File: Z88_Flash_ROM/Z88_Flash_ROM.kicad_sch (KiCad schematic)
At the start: 3 parts, among them J1 Conn_01x03, U1 SST39SF040, U2 Z88_ROM

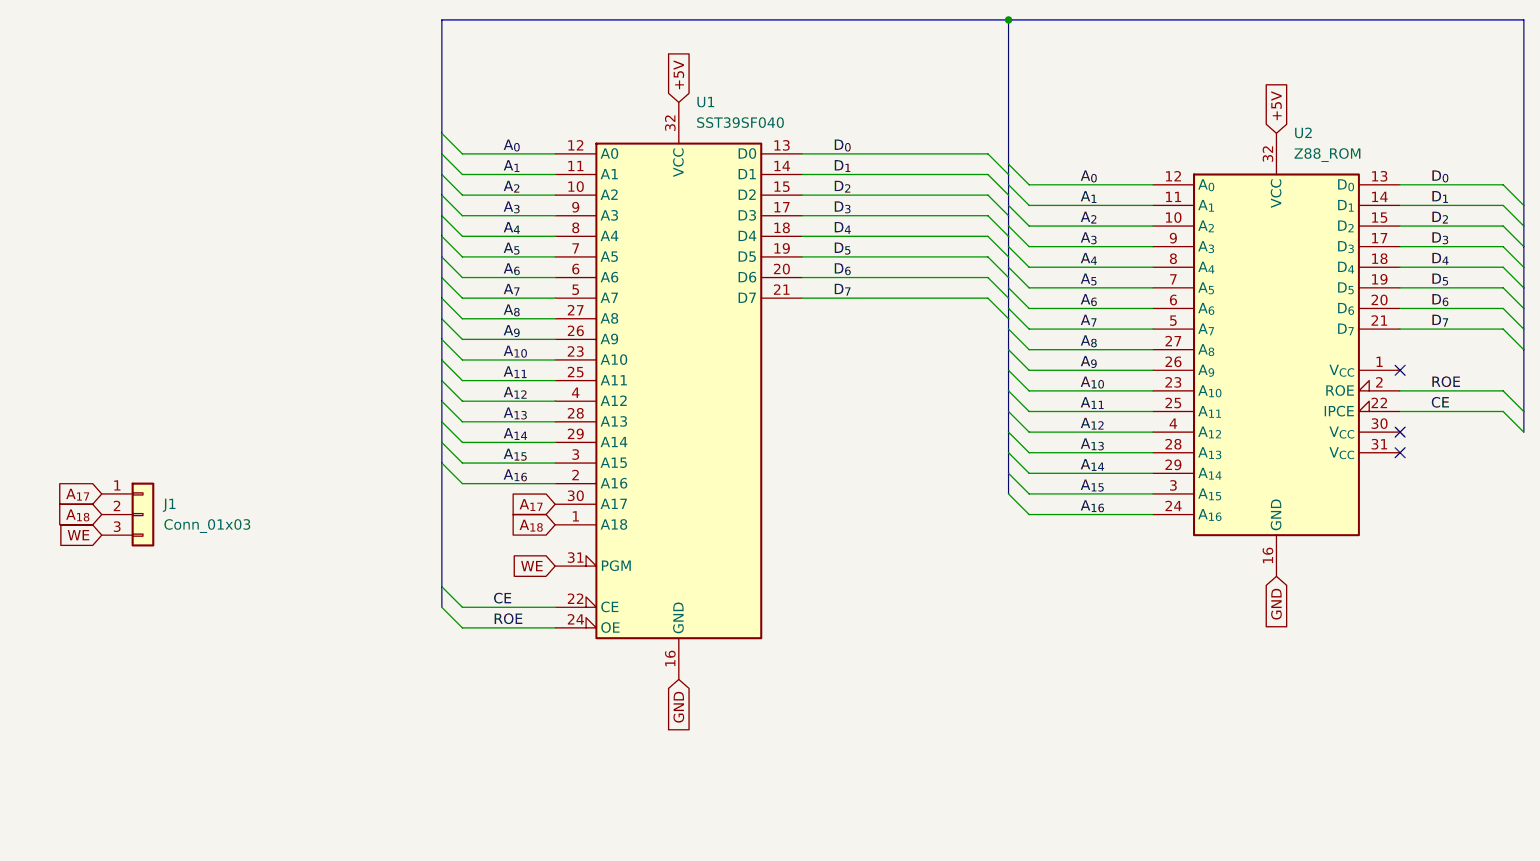
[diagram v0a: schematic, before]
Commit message: Reduced PCB thickness
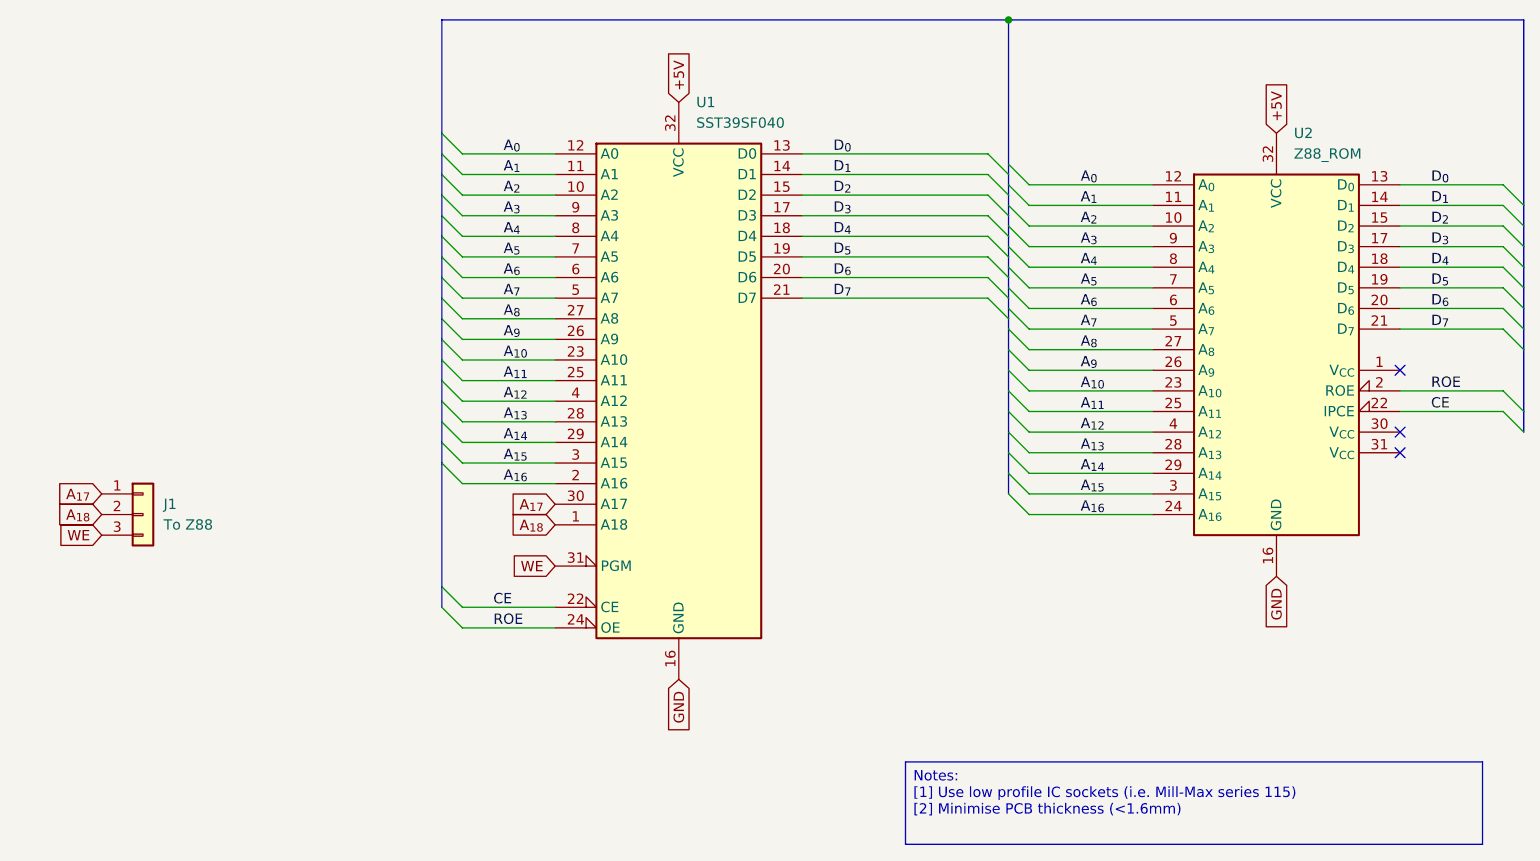
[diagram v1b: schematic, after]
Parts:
- J1: value Conn_01x03 -> To Z88
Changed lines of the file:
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@@
 		(comment 1 "www.youtube.com/@Brfff")
+	)
+	(text_box "Notes:\n[1] Use low profile IC sockets (i.e. Mill-Max series 115)\n[2] Minimise PCB thickness (<1.6mm)"
+		(exclude_from_sim no)
+		(at 140.97 142.24 0)
+		(size 71.12 10.16)
+		(margins 0.9525 0.9525 0.9525 0.9525)
+		(stroke
+			(width 0)
+			(type solid)
+		)
+		(fill
+			(type none)
+		)
+		(effects
+			(font
+				(size 1.27 1.27)
+			)
+			(justify left top)
+		)
 	)
 	(junction
@@
 			)
 		)
-		(property "Value" "Conn_01x03"
+		(property "Value" "To Z88"
 			(at 49.53 113.0299 0)
 			(effects
